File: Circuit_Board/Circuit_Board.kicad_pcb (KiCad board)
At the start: 4 copper layers, 90.2 x 71.9 mm, 41 parts, among them J1 Conn_01x02, J2 Control stuff, J3 Power stuff, J4 Conn_02x06_Odd_Even, J5 Conn_01x20_Socket, J6 Conn_01x20_Socket, J7 GPIO_1, J8 GPIO_2, J9 LED_AMP, Q2 IRF540N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

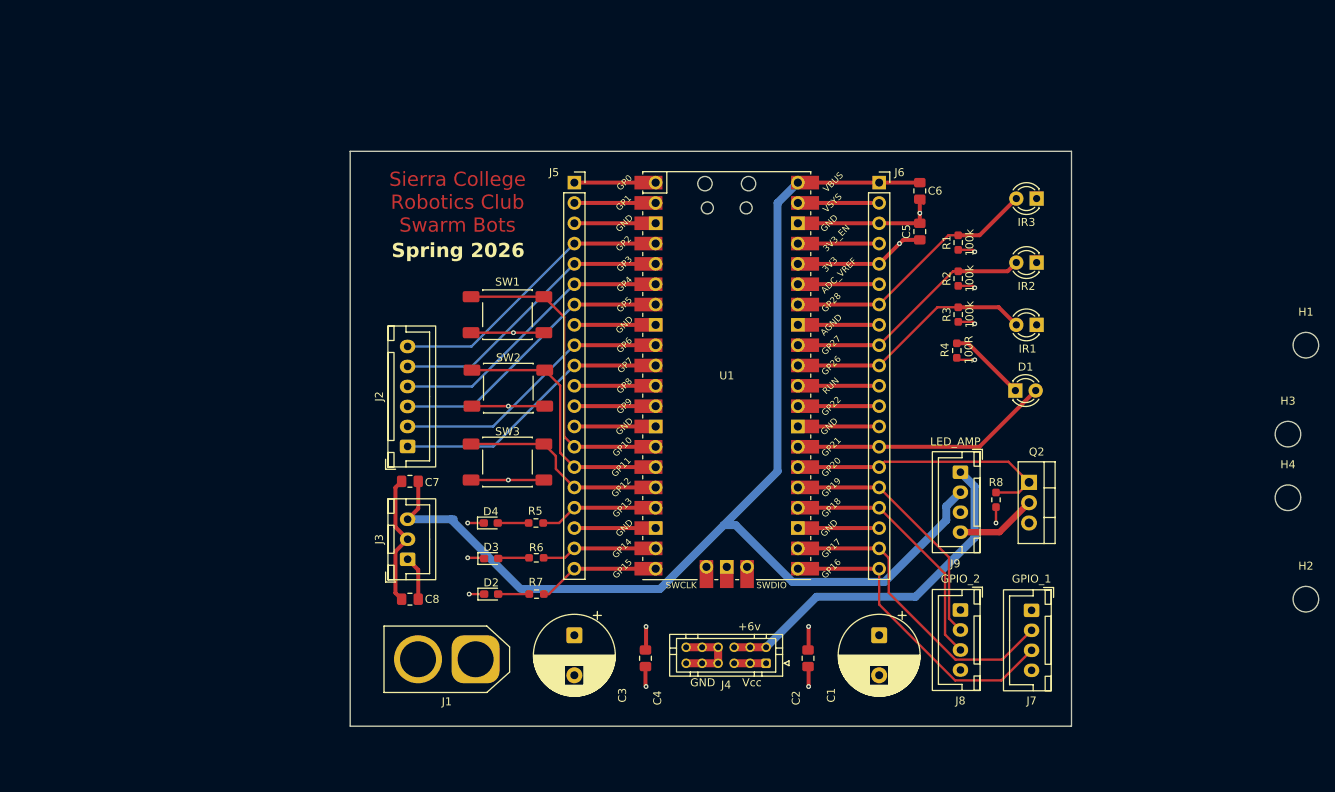
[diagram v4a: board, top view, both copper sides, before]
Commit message: Added mounting hole to PCB
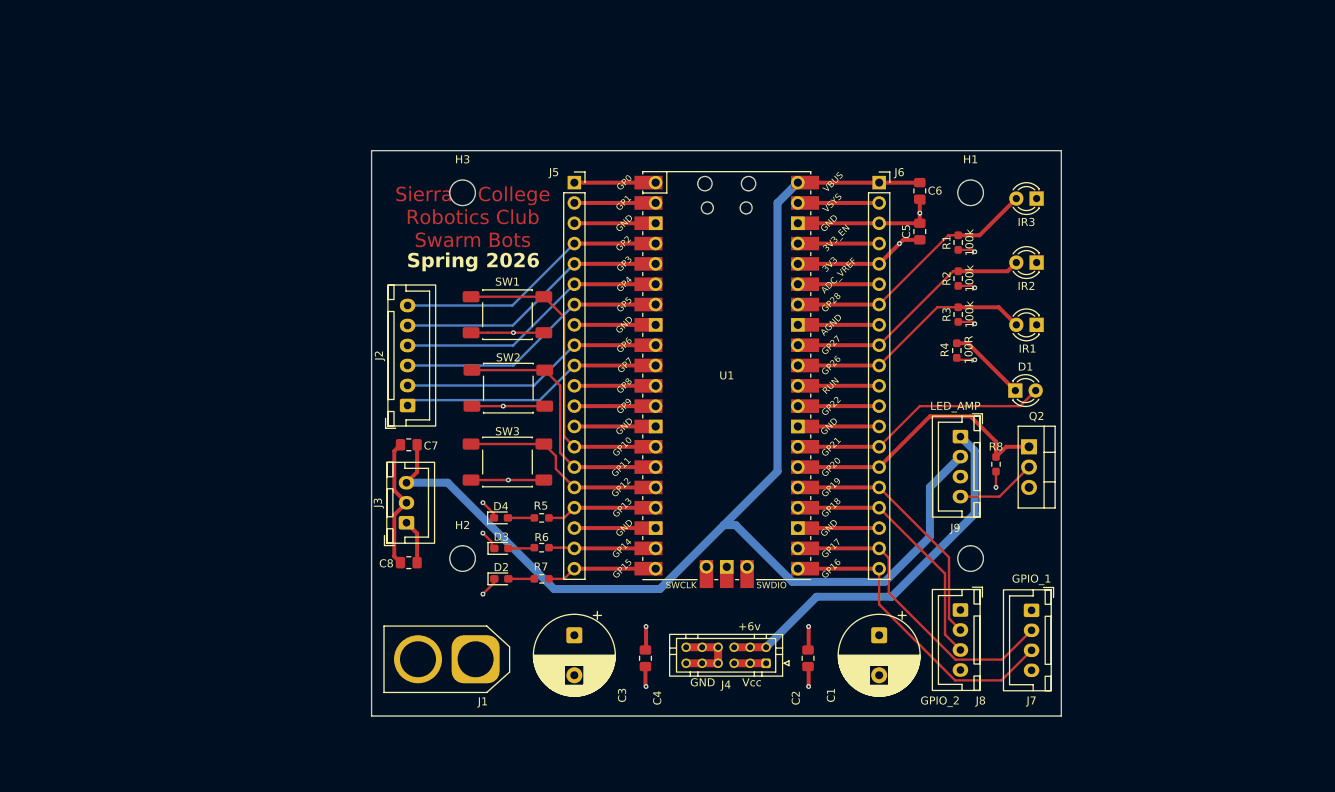
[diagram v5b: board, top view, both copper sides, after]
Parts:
- moved H3 107.5 mm to (114.3, 71.1)
- moved H2 105.5 mm to (114.3, 116.8)
- moved H1 46.0 mm to (177.8, 71.1)
- moved H4 40.4 mm to (177.8, 116.8)
- moved J2 5.12 mm to (107.4, 97.7)
- moved J3 4.57 mm to (107.3, 112.4)
- moved C7 4.57 mm to (107.6, 102.6)
- moved C8 4.57 mm to (107.6, 117.4)
- moved J9 4.45 mm to (176.5, 101.6)
- moved R8 4.45 mm to (181.0, 105.1)
- moved Q2 4.44 mm to (185.1, 102.9)
- moved D2 2.29 mm to (119.1, 119.4)
- moved R7 2.01 mm to (124.2, 119.4)
- moved D3 1.80 mm to (119.1, 115.6)
- moved R6 1.43 mm to (124.2, 115.5)
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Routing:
- net VBUS: track 151.8 -> 158.3 mm
- net +6V: track 66.9 -> 69.6 mm
- net GND: track 112.6 -> 114.5 mm
- net Net-(J2-Pin_5): track 35.8 -> 34.2 mm
- net Net-(J2-Pin_3): track 35.8 -> 34.2 mm
- net Net-(J2-Pin_2): track 34.7 -> 33.1 mm
- net Net-(J2-Pin_6): track 35.8 -> 34.2 mm
- net Net-(J2-Pin_4): track 35.8 -> 34.2 mm
- net Net-(J2-Pin_1): track 34.7 -> 33.1 mm
- net Net-(J5-Pin_20): track 15.3 -> 13.9 mm
- net Net-(J5-Pin_19): track 14.5 -> 13.4 mm
- net Net-(J5-Pin_17): track 14.8 -> 13.9 mm
- net Net-(D2-A): track 3.89 -> 3.25 mm
- net Net-(D4-A): track 3.86 -> 3.30 mm
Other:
- board size 90.2 x 71.9 mm -> 86.2 x 70.7 mm

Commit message: finalized pcb layout
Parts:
- R4: value 100R -> 100k
- moved D2 0.49 mm to (119.6, 119.4)
- moved D3 0.49 mm to (119.6, 115.6)
- moved D4 0.49 mm to (119.6, 111.8)
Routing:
- net GND: track 114.5 -> 115.2 mm
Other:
- board size 86.2 x 70.7 mm -> 86 x 70.5 mm
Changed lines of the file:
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@@
 			(at 0 -4.15 0)
 			(layer "F.SilkS")
+			(hide yes)
 			(effects
 				(font
@@
 		(tags "capacitor handsolder")
 		(property "Reference" "C4"
-			(at 4.9625 -1.5 90)
+			(at 0.2325 -1.905 90)
 			(layer "F.SilkS")
 			(effects
@@
 			(at -0.5 -1.5 90)
 			(layer "F.Fab")
+			(hide yes)
 			(effects
 				(font
@@
 		(tags "capacitor handsolder")
 		(property "Reference" "C8"
-			(at 2.80125 -0.11875 0)
+			(at 2.92825 -0.11875 0)
 			(layer "F.SilkS")
 			(effects
@@
 		(tags "capacitor handsolder")
 		(property "Reference" "C2"
-			(at 4.9625 1.5 90)
+			(at 0.2325 1.5 90)
 			(layer "F.SilkS")
 			(effects
@@
 			(at -0.5 1.68 90)
 			(layer "F.Fab")
+			(hide yes)
 			(effects
 				(font
@@
 		)
 		(property "Value" "SW_Push"
-			(at 0 -3.81 0)
+			(at -0.494 -3.81 0)
 			(layer "F.Fab")
 			(effects
@@
 		(tags "capacitor handsolder")
 		(property "Reference" "C7"
-			(at -2.7725 -0.127 0)
+			(at 2.92825 -0.127 0)
 			(layer "F.SilkS")
 			(effects
@@
 	(footprint "LED_SMD:LED_0603_1608Metric_Pad1.05x0.95mm_HandSolder"
 		(layer "F.Cu")
-		(at 119.0925 111.76)
+		(at 119.5865 111.76)
 		(descr "LED SMD 0603 (1608 Metric), square (rectangular) end terminal, IPC-7351 nominal, (Body size source: http://www.tortai-tech.com/upload/download/2011102023233369053.pdf)")
 		(tags "LED handsolder")
@@
 		)
 		(fp_text user "SWCLK"
-			(at -5.7 26.2 0)
+			(at -5.715 26.67 180)
 			(layer "F.SilkS")
 			(effects
@@
 		)
 		(fp_text user "SWDIO"
-			(at 5.6 26.2 0)
+			(at 5.6 26.67 180)
 			(layer "F.SilkS")
 			(effects
@@
 			(at 0 -4.15 0)
 			(layer "F.SilkS")
+			(hide yes)
 			(effects
 				(font
@@
 		)
 		(property "Value" "MountingHole"
-			(at 0 4.15 0)
+			(at -4.445 3.81 0)
 			(layer "F.Fab")
 			(effects
@@
 	(footprint "LED_SMD:LED_0603_1608Metric_Pad1.05x0.95mm_HandSolder"
 		(layer "F.Cu")
-		(at 119.14 119.38)
+		(at 119.634 119.38)
 		(descr "LED SMD 0603 (1608 Metric), square (rectangular) end terminal, IPC-7351 nominal, (Body size source: http://www.tortai-tech.com/upload/download/2011102023233369053.pdf)")
 		(tags "LED handsolder")
@@
 			)
 		)
-		(property "Value" "100R"
+		(property "Value" "100k"
 			(at 0.0875 1.5 90)
 			(layer "F.SilkS")
@@
 	(footprint "LED_SMD:LED_0603_1608Metric_Pad1.05x0.95mm_HandSolder"
 		(layer "F.Cu")
-		(at 119.14 115.57)
+		(at 119.634 115.57)
 		(descr "LED SMD 0603 (1608 Metric), square (rectangular) end terminal, IPC-7351 nominal, (Body size source: http://www.tortai-tech.com/upload/download/2011102023233369053.pdf)")
 		(tags "LED handsolder")
@@
 			(at 0 -4.15 0)
 			(layer "F.SilkS")
+			(hide yes)
 			(effects
 				(font
@@
 	)
 	(gr_rect
-		(start 102.923485 65.857581)
-		(end 189.142667 136.525)
+		(start 103 66)
+		(end 189 136.5)
 		(stroke
 			(width 0.05)
-			(type default)
+			(type solid)
 		)
 		(fill no)
@@
 	)
 	(segment
-		(start 117.9475 114.7725)
-		(end 117.9475 115.48)
+		(start 118.7115 110.5835)
+		(end 117.348 109.22)
 		(width 0.3)
 		(layer "F.Cu")
@@
 	)
 	(segment
-		(start 118.2175 111.76)
-		(end 118.2175 111.2325)
+		(start 118.4415 114.7725)
+		(end 118.4415 115.48)
 		(width 0.3)
 		(layer "F.Cu")
@@
 	)
 	(segment
+		(start 118.7115 111.76)
+		(end 118.7115 110.5835)
+		(width 0.3)
+		(layer "F.Cu")
+		(net "GND")
+	)
+	(segment
 		(start 105.76125 108.34125)
 		(end 107.28625 109.86625)
@@
 	)
 	(segment
-		(start 118.265 119.86)
-		(end 118.265 119.38)
+		(start 118.759 119.86)
+		(end 118.759 119.38)
 		(width 0.3)
 		(layer "F.Cu")
@@
 	)
 	(segment
-		(start 116.84 113.665)
-		(end 117.9475 114.7725)
+		(start 117.334 113.665)
+		(end 118.4415 114.7725)
 		(width 0.3)
 		(layer "F.Cu")
@@
 	)
 	(segment
-		(start 118.2175 111.2325)
-		(end 116.84 109.855)
-		(width 0.3)
-		(layer "F.Cu")
-		(net "GND")
-	)
-	(segment
 		(start 115.36 88.61)
 		(end 117.475 88.61)
@@
 	)
 	(segment
-		(start 116.84 121.285)
-		(end 118.265 119.86)
+		(start 117.334 121.285)
+		(end 118.759 119.86)
 		(width 0.3)
 		(layer "F.Cu")
@@
 	)
 	(via
-		(at 116.84 109.855)
+		(at 117.348 109.22)
 		(size 0.6)
 		(drill 0.3)
@@
 	)
 	(via
-		(at 116.84 113.665)
+		(at 117.334 113.665)
 		(size 0.6)
 		(drill 0.3)
@@
 	)
 	(via
-		(at 116.84 121.285)
+		(at 117.334 121.285)
 		(size 0.6)
 		(drill 0.3)
@@
 	)
 	(segment
-		(start 153.67 105.941726)
-		(end 153.67 72.39)
+		(start 113.20825 107.36625)
+		(end 126.492 120.65)
 		(width 1)
 		(layer "B.Cu")
@@
 	)
 	(segment
-		(start 167.053453 119.76)
-		(end 172.72 114.093453)
-		(width 1)
-		(layer "B.Cu")
-		(net "VBUS")
-	)
-	(segment
-		(start 138.961726 120.65)
-		(end 146.950863 112.660863)
+		(start 153.67 105.941726)
+		(end 153.67 72.39)
 		(width 1)
 		(layer "B.Cu")
@@
 	)
 	(segment
-		(start 125.73 120.65)
-		(end 112.44625 107.36625)
+		(start 167.053453 119.76)
+		(end 172.72 114.093453)
 		(width 1)
 		(layer "B.Cu")
@@
 	)
 	(segment
-		(start 172.72 107.91)
-		(end 176.53 104.1)
+		(start 107.28625 107.36625)
+		(end 113.20825 107.36625)
 		(width 1)
 		(layer "B.Cu")
@@
 	)
 	(segment
-		(start 125.73 120.65)
+		(start 126.492 120.65)
 		(end 138.961726 120.65)
 		(width 1)
@@
 	)
 	(segment
-		(start 112.44625 107.36625)
-		(end 107.28625 107.36625)
+		(start 172.72 107.91)
+		(end 176.53 104.1)
+		(width 1)
+		(layer "B.Cu")
+		(net "VBUS")
+	)
+	(segment
+		(start 138.961726 120.65)
+		(end 146.950863 112.660863)
 		(width 1)
 		(layer "B.Cu")
@@
 	)
 	(segment
-		(start 120.015 115.57)
+		(start 120.509 115.57)
 		(end 123.18 115.57)
 		(width 0.3)
@@
 	)
 	(segment
-		(start 120.015 115.57)
-		(end 120.105 115.48)
+		(start 120.509 115.57)
+		(end 120.599 115.48)
 		(width 0.3)
 		(layer "F.Cu")
@@
 	)
 	(segment
-		(start 119.9675 111.76)
+		(start 120.4615 111.76)
 		(end 123.27 111.76)
 		(width 0.3)
@@
 	)
 	(segment
-		(start 120.015 119.38)
+		(start 120.509 119.38)
 		(end 123.27 119.38)
 		(width 0.3)

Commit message: Made final changes to schmatic and PCB
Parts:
- added G***: LOGO, Project_lib:Ref_Proto, F.Cu at (147.3, 94.0)
- added G***: LOGO, Project_lib:Ref_Proto, B.Cu at (147.3, 94.0)
- C7: value C_Polarized -> 0.1uF
- C8: value C_Polarized -> 0.33uF
- moved R8 1.06 mm to (181.0, 104.0)
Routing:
- net /FET_GATE: track 35.3 -> 33.1 mm
- net GND: vias 14 -> 79
- added copper zone on B.Cu, net GND
- added copper zone on F.Cu, net GND
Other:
- board text added: "1. 2. 3. 4."
- board text added: "1.3V3 2.GPIO:19/17 3.GPIO:18/16 4.GND"
- board text added: "6/12Vin"
- board text added: "6V 5V 3V3 SW_G"
- board text added: "Motor Controller I/O"
- board text added: "VREG or Motor PWR"

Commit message: PCB Rev 1.1: Resistor value and silkscreen corrections
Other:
- board text added: "Designed by: Jense Duart Patrick Leiser v1.1"
- board text removed: "Designed by: Jense Daurt Patrick Leiser v1.0"
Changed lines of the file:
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@@
 		)
 	)
-	(gr_text "Designed by: \nJense Daurt\nPatrick Leiser\nv1.0"
+	(gr_text "Designed by: \nJense Duart\nPatrick Leiser\nv1.1"
 		(at 122.174 83.058 0)
 		(layer "B.SilkS")
